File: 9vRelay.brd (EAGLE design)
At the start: 20 x 24 mm, 6 parts, among them K1 OJE-SS-109LMH, T1 2N3904

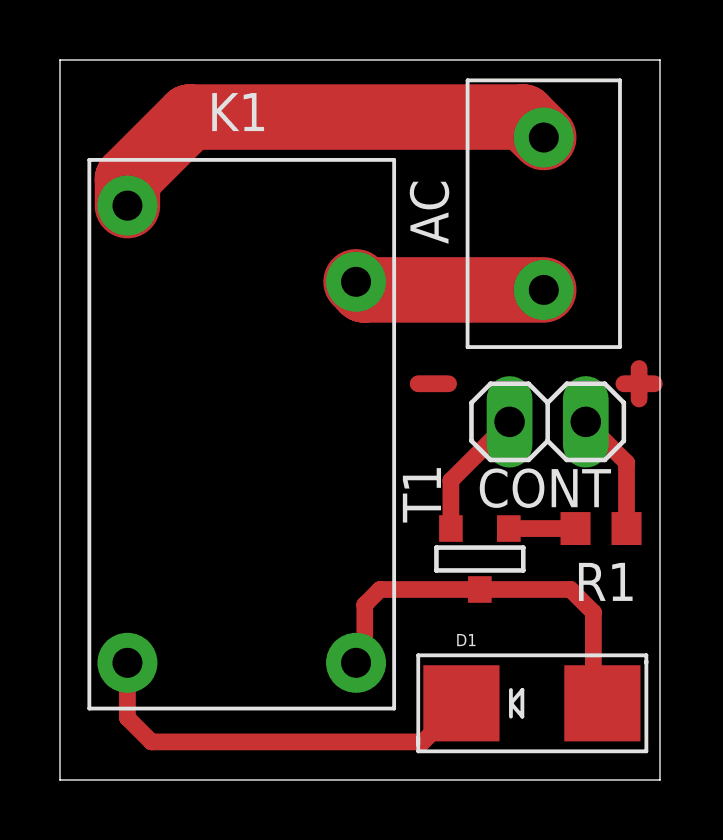
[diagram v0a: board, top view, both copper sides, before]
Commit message: Re orientation and fixes
Re orientation and fixed the missing input voltage for powering the relay coil
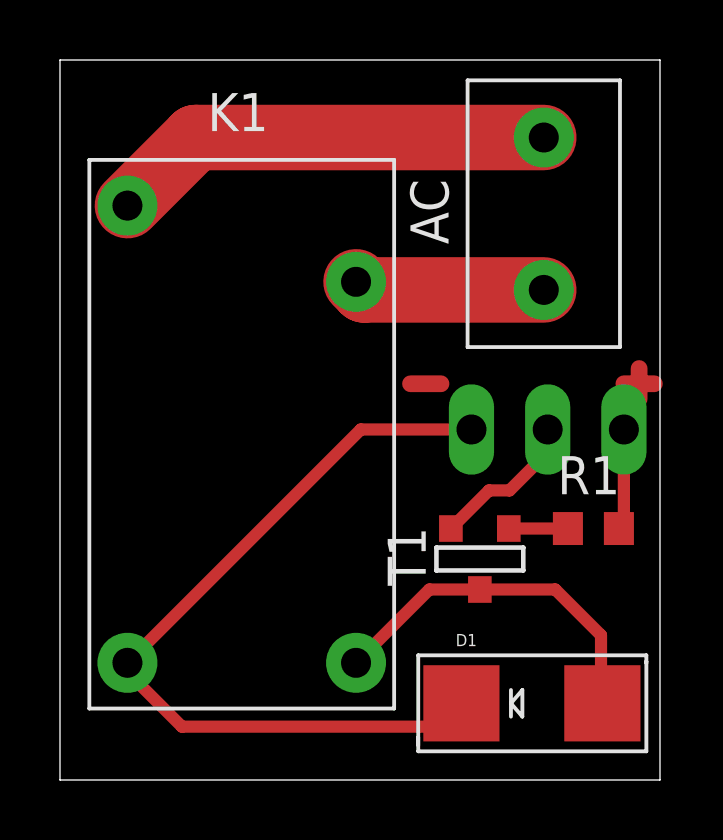
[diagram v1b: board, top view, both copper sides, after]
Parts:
- removed CONT: (no value), pinhead:1X02
- added X1: 22-23-2031, con-molex:22-23-2031
- moved R1 0.25 mm to (17.8, 8.38), turned to 180 degrees
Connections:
- removed net N$4 (its old number): D1.C, K1.1
- removed net N$6: CONT.2, T1.2
- new net N$2: D1.C, K1.1, X1.3
- new net N$3: R1.1, X1.1
- net N$7: now also T1.2, X1.2; no longer CONT.1, R1.2
- net N$8: now also R1.2; no longer R1.1
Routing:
- net N$2: track 0.00 -> 27.2 mm
- net N$4 (its old number): track 13.8 -> 0.00 mm
- net N$6: track 4.37 -> 0.00 mm
- net N$3: track 0.00 -> 3.37 mm
- net N$1: track 13.4 -> 12.1 mm
- net N$4: track 15.9 -> 14.8 mm
- net N$7: track 4.12 -> 5.04 mm
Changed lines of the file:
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@@
 <?xml version="1.0" encoding="utf-8"?>
 <!DOCTYPE eagle SYSTEM "eagle.dtd">
-<eagle version="7.3.0">
+<eagle version="7.4.0">
 <drawing>
 <settings>
@@
 <wire x1="20" y1="24" x2="0" y2="24" width="0" layer="20"/>
 <wire x1="0" y1="24" x2="0" y2="0" width="0" layer="20"/>
+<dimension x1="0" y1="24" x2="0" y2="0" x3="-4.064" y3="12" textsize="1.778" layer="1"/>
+<dimension x1="0" y1="24" x2="20" y2="24" x3="10" y3="25.908" textsize="1.778" layer="1"/>
 </plain>
 <attributes>
@@
 <attribute name="MF" value="" x="13.97" y="7.366" size="1.778" layer="27" display="off"/>
 <attribute name="OC_NEWARK" value="unknown" x="13.97" y="7.366" size="1.778" layer="27" display="off"/>
-<attribute name="NAME" x="11.43" y="10.541" size="1.27" layer="25" ratio="10" rot="R270"/>
-</element>
-<element name="CONT" library="pinhead" package="1X02" value="" x="16.256" y="11.938" smashed="yes" rot="R180">
-<attribute name="NAME" x="18.3642" y="10.3632" size="1.27" layer="25" ratio="10" rot="R180"/>
-<attribute name="VALUE" x="18.796" y="15.113" size="1.27" layer="27" rot="R180"/>
+<attribute name="NAME" x="12.192" y="6.477" size="1.27" layer="25" ratio="10" rot="R90"/>
 </element>
 <element name="AC" library="userdefined" package="TBLOCK1X2" value="TBLOCK1X2" x="16.126" y="18.876" smashed="yes" rot="R90">
 <attribute name="NAME" x="12.951" y="17.86" size="1.27" layer="21" rot="R90"/>
 </element>
-<element name="R1" library="resistor" package="R0603" value="" x="18.034" y="8.382" smashed="yes">
-<attribute name="NAME" x="17.145" y="5.969" size="1.27" layer="25"/>
-<attribute name="VALUE" x="17.399" y="6.477" size="1.27" layer="27"/>
+<element name="R1" library="resistor" package="R0603" value="" x="17.78" y="8.382" smashed="yes" rot="R180">
+<attribute name="NAME" x="18.669" y="10.795" size="1.27" layer="25" rot="R180"/>
+<attribute name="VALUE" x="18.415" y="10.287" size="1.27" layer="27" rot="R180"/>
 </element>
 <element name="D1" library="adafruit" package="SMADIODE" value="" x="15.73" y="2.556"/>
+<element name="X1" library="con-molex" package="22-23-2031" value="22-23-2031" x="16.256" y="11.684" smashed="yes" rot="MR0">
+<attribute name="MF" value="MOLEX" x="16.256" y="11.684" size="1.778" layer="28" rot="MR0" display="off"/>
+<attribute name="MPN" value="22-23-2031" x="16.256" y="11.684" size="1.778" layer="28" rot="MR0" display="off"/>
+<attribute name="OC_NEWARK" value="30C0862" x="16.256" y="11.684" size="1.778" layer="28" rot="MR0" display="off"/>
+<attribute name="OC_FARNELL" value="1462950" x="16.256" y="11.684" size="1.778" layer="28" rot="MR0" display="off"/>
+</element>
 </elements>
 <signals>
+<signal name="N$5">
+<wire x1="19.304" y1="13.716" x2="19.304" y2="12.7" width="0.5588" layer="1"/>
+</signal>
+<signal name="N$9">
+<wire x1="18.796" y1="13.208" x2="19.812" y2="13.208" width="0.5588" layer="1"/>
+</signal>
+<signal name="N$10">
+<wire x1="11.684" y1="13.208" x2="12.7" y2="13.208" width="0.5588" layer="1"/>
+</signal>
+<signal name="N$7">
+<contactref element="T1" pad="2"/>
+<contactref element="X1" pad="2"/>
+<wire x1="16.256" y1="11.684" x2="16.256" y2="10.922" width="0.4064" layer="1"/>
+<wire x1="16.256" y1="10.922" x2="14.986" y2="9.652" width="0.4064" layer="1"/>
+<wire x1="14.986" y1="9.652" x2="14.3002" y2="9.652" width="0.4064" layer="1"/>
+<wire x1="14.3002" y1="9.652" x2="13.0302" y2="8.382" width="0.4064" layer="1"/>
+</signal>
+<signal name="N$8">
+<contactref element="R1" pad="2"/>
+<contactref element="T1" pad="3"/>
+<wire x1="14.9606" y1="8.382" x2="16.93" y2="8.382" width="0.4064" layer="1"/>
+</signal>
 <signal name="N$1">
+<contactref element="K1" pad="2"/>
+<contactref element="T1" pad="1"/>
+<contactref element="D1" pad="A"/>
+<wire x1="18.0795" y1="2.556" x2="18.034" y2="2.6015" width="0.4064" layer="1"/>
+<wire x1="18.034" y1="2.6015" x2="18.034" y2="4.826" width="0.4064" layer="1"/>
+<wire x1="18.034" y1="4.826" x2="16.51" y2="6.35" width="0.4064" layer="1"/>
+<wire x1="16.51" y1="6.35" x2="13.9954" y2="6.35" width="0.4064" layer="1"/>
+<wire x1="13.9954" y1="6.35" x2="12.312" y2="6.35" width="0.4064" layer="1"/>
+<wire x1="12.312" y1="6.35" x2="9.868" y2="3.906" width="0.4064" layer="1"/>
+</signal>
+<signal name="N$2">
+<contactref element="K1" pad="1"/>
+<contactref element="D1" pad="C"/>
+<contactref element="X1" pad="3"/>
+<wire x1="13.3805" y1="2.556" x2="12.6025" y2="1.778" width="0.4064" layer="1"/>
+<wire x1="12.6025" y1="1.778" x2="4.064" y2="1.778" width="0.4064" layer="1"/>
+<wire x1="4.064" y1="1.778" x2="2.248" y2="3.594" width="0.4064" layer="1"/>
+<wire x1="2.248" y1="3.594" x2="2.248" y2="3.906" width="0.4064" layer="1"/>
+<wire x1="13.716" y1="11.684" x2="10.026" y2="11.684" width="0.4064" layer="1"/>
+<wire x1="10.026" y1="11.684" x2="2.248" y2="3.906" width="0.4064" layer="1"/>
+</signal>
+<signal name="N$4">
+<contactref element="K1" pad="4"/>
 <contactref element="AC" pad="2"/>
-<contactref element="K1" pad="4"/>
-<wire x1="16.126" y1="21.416" x2="15.444" y2="22.098" width="2.1844" layer="1"/>
-<wire x1="15.444" y1="22.098" x2="4.318" y2="22.098" width="2.1844" layer="1"/>
-<wire x1="4.318" y1="22.098" x2="2.248" y2="20.028" width="2.1844" layer="1"/>
-<wire x1="2.248" y1="20.028" x2="2.248" y2="19.146" width="2.1844" layer="1"/>
-</signal>
-<signal name="N$2">
+<wire x1="2.248" y1="19.146" x2="4.518" y2="21.416" width="2.1844" layer="1"/>
+<wire x1="4.518" y1="21.416" x2="16.126" y2="21.416" width="2.1844" layer="1"/>
+</signal>
+<signal name="N$3">
+<contactref element="X1" pad="1"/>
+<contactref element="R1" pad="1"/>
+<wire x1="18.796" y1="11.684" x2="18.796" y2="8.548" width="0.4064" layer="1"/>
+<wire x1="18.796" y1="8.548" x2="18.63" y2="8.382" width="0.4064" layer="1"/>
+</signal>
+<signal name="N$11">
+<contactref element="AC" pad="1"/>
 <contactref element="K1" pad="3"/>
-<contactref element="AC" pad="1"/>
 <wire x1="9.868" y1="16.606" x2="10.138" y2="16.336" width="2.1844" layer="1"/>
 <wire x1="10.138" y1="16.336" x2="16.126" y2="16.336" width="2.1844" layer="1"/>
 </signal>
-<signal name="N$3">
-<contactref element="T1" pad="1"/>
-<contactref element="K1" pad="2"/>
-<contactref element="D1" pad="A"/>
-<wire x1="9.868" y1="3.906" x2="10.16" y2="4.198" width="0.5588" layer="1"/>
-<wire x1="10.16" y1="4.198" x2="10.16" y2="5.842" width="0.5588" layer="1"/>
-<wire x1="10.16" y1="5.842" x2="10.668" y2="6.35" width="0.5588" layer="1"/>
-<wire x1="10.668" y1="6.35" x2="13.9954" y2="6.35" width="0.5588" layer="1"/>
-<wire x1="18.0795" y1="2.556" x2="17.78" y2="2.8555" width="0.5588" layer="1"/>
-<wire x1="17.78" y1="2.8555" x2="17.78" y2="5.588" width="0.5588" layer="1"/>
-<wire x1="17.78" y1="5.588" x2="17.018" y2="6.35" width="0.5588" layer="1"/>
-<wire x1="17.018" y1="6.35" x2="13.9954" y2="6.35" width="0.5588" layer="1"/>
-</signal>
-<signal name="N$4">
-<contactref element="D1" pad="C"/>
-<contactref element="K1" pad="1"/>
-<wire x1="13.3805" y1="2.556" x2="12.0945" y2="1.27" width="0.5588" layer="1"/>
-<wire x1="12.0945" y1="1.27" x2="3.048" y2="1.27" width="0.5588" layer="1"/>
-<wire x1="3.048" y1="1.27" x2="2.248" y2="2.07" width="0.5588" layer="1"/>
-<wire x1="2.248" y1="2.07" x2="2.248" y2="3.906" width="0.5588" layer="1"/>
-</signal>
-<signal name="N$6">
-<contactref element="T1" pad="2"/>
-<contactref element="CONT" pad="2"/>
-<wire x1="13.0302" y1="8.382" x2="13.0302" y2="9.9822" width="0.5588" layer="1"/>
-<wire x1="13.0302" y1="9.9822" x2="14.986" y2="11.938" width="0.5588" layer="1"/>
-</signal>
-<signal name="N$7">
-<contactref element="CONT" pad="1"/>
-<contactref element="R1" pad="2"/>
-<wire x1="18.884" y1="8.382" x2="18.884" y2="10.58" width="0.5588" layer="1"/>
-<wire x1="18.884" y1="10.58" x2="17.526" y2="11.938" width="0.5588" layer="1"/>
-</signal>
-<signal name="N$8">
-<contactref element="R1" pad="1"/>
-<contactref element="T1" pad="3"/>
-<wire x1="14.9606" y1="8.382" x2="17.184" y2="8.382" width="0.5588" layer="1"/>
-</signal>
-<signal name="N$5">
-<wire x1="19.304" y1="13.716" x2="19.304" y2="12.7" width="0.5588" layer="1"/>
-</signal>
-<signal name="N$9">
-<wire x1="18.796" y1="13.208" x2="19.812" y2="13.208" width="0.5588" layer="1"/>
-</signal>
-<signal name="N$10">
-<wire x1="11.938" y1="13.208" x2="12.954" y2="13.208" width="0.5588" layer="1"/>
-</signal>
 </signals>
